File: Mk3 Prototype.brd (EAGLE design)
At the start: 107 x 53.5 mm, 132 parts, among them IC1 STM32F401R, IC2 CC3100, IC3 S25FL216K0PMFI011, J1 ZX62-AB-5PA(11), J2 SWD_SHROUD_SMD, J4 Arduino Headers, J7 SFV30R-2STE1HLF, Q1 BSS84W, Q10 2N7002KW, Q11 BSS84W, Q12 2N7002KW, U1 USD-SOCKETNEW, U2 JHD12864-G13BSW-OUTLINE, U3 MCP73831, X1 ABS07-32.768KHZ-T, X2 Q24FA20H00396, X3 CRYSTAL-3.2-2.5, X4 ABS07-32.768KHZ-T, Y1 AH316M245001-T

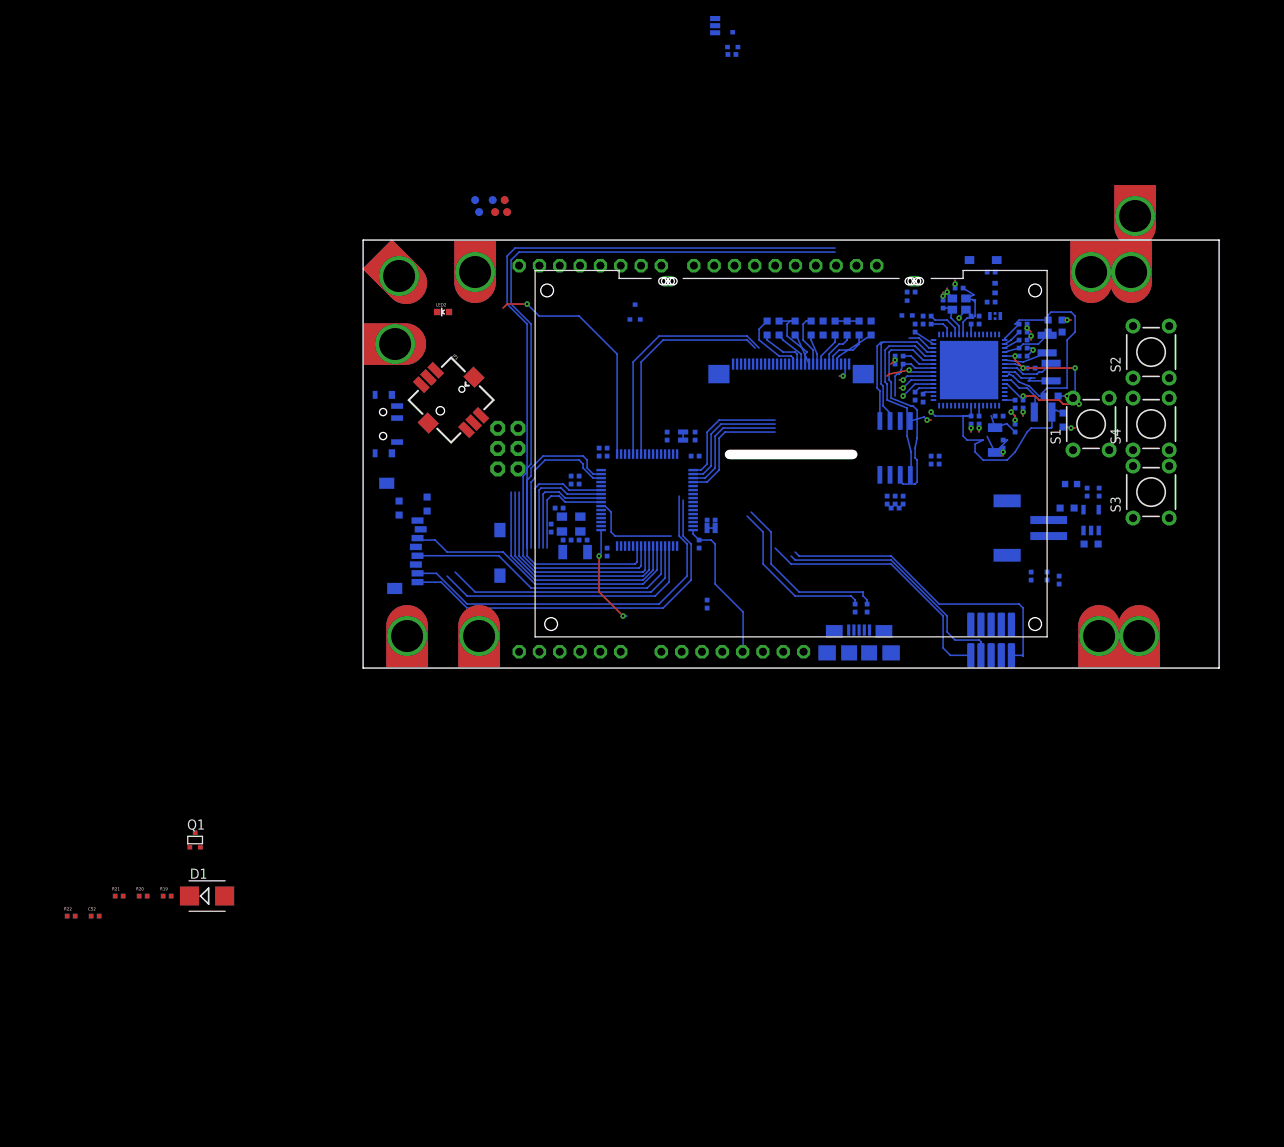
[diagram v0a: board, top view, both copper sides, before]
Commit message: Lots of schematic clean up
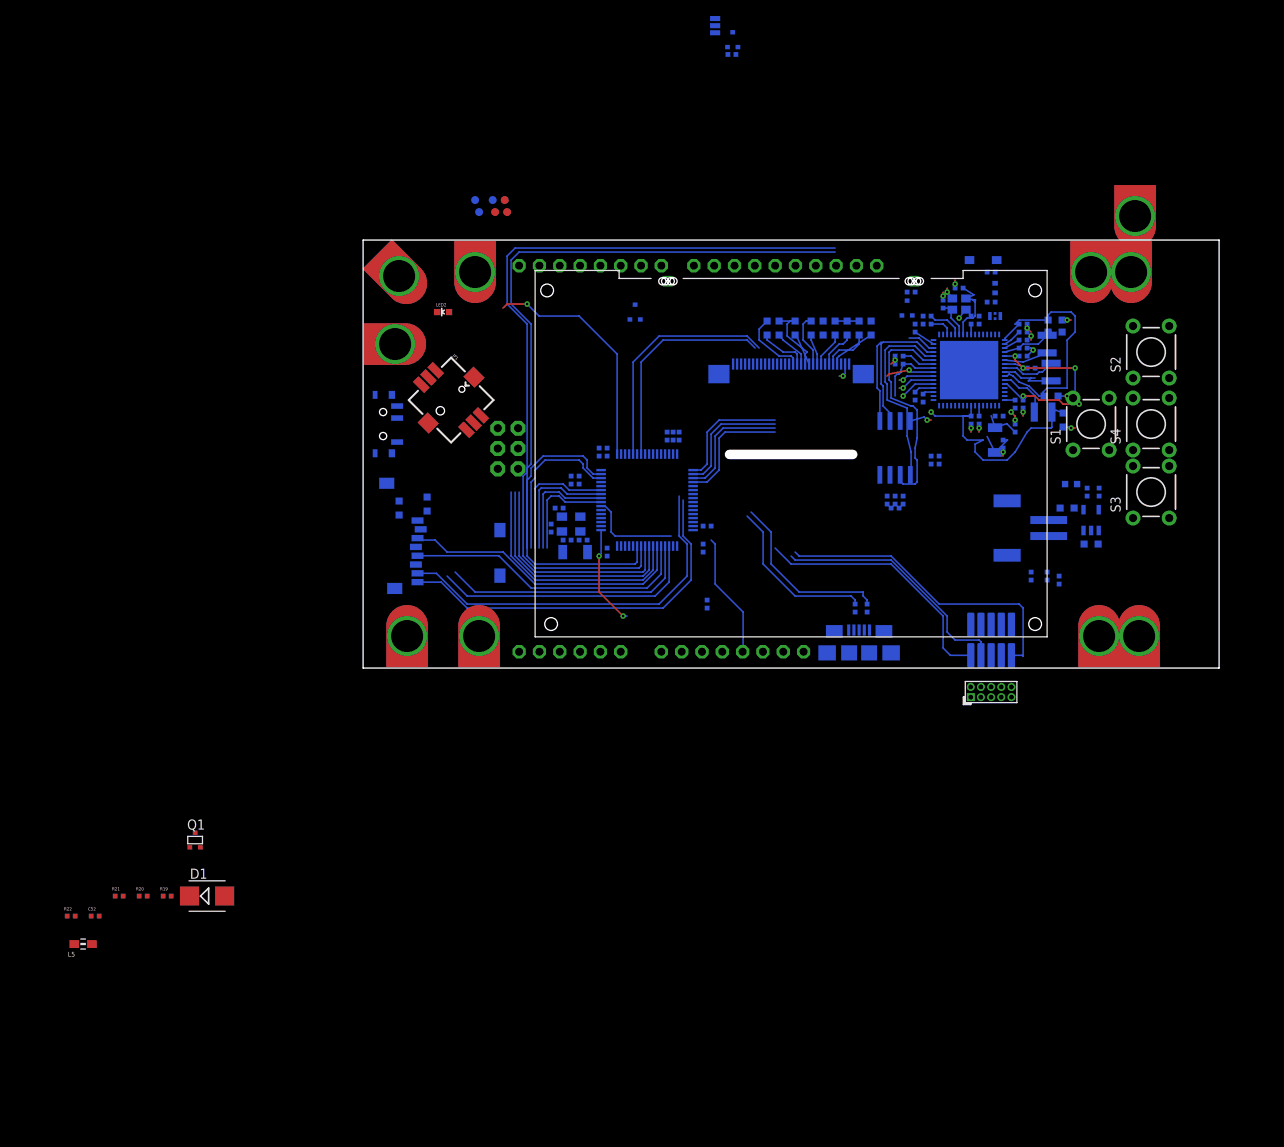
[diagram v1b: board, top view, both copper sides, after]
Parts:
- removed SJ1, SJ2: SOLDERJUMPERTRACE, TiLDA Mk3 Parts:SJ_2S-TRACE
- added JP3: (no value), TiLDA Mk3 Parts:PINHEAD_2X05_127
- added L5: Bead, TiLDA Mk3 Parts:WUERTH-0805
- C34: value 1u -> 0402/1u/10V/X5R
- C35, C36: value 12p -> 0402/12p/50V/NP0
- C48, C49: value nc -> 0402/0R
- R12, R13, R14: value 100K -> 0402/100K/5%
- moved C7 13.7 mm to (39.5, 29.0), turned to 270 degrees
- moved C9 11.5 mm to (42.5, 15.0), turned to 90 degrees
- moved C49 11.5 mm to (38.8, 29.0), turned to 270 degrees
- moved C48 11.3 mm to (43.0, 17.8), turned to 0 degrees
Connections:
- net DM renamed D_N
- net DP renamed D_P
- net N$29 renamed USB_D_N
- net N$30 renamed USB_D_P
- net N$43 renamed OCS32_IN
- net N$45 renamed OCS32_OUT
- new net N$29: L5.1
- new net N$30: IC1.43
- new net N$39: IC1.22
- new net N$43: IC1.24
- new net N$45: IC1.25
- new net N$48: IC1.20
- new net N$49: IC1.16
- new net N$50: IC1.50
- new net N$51: IC1.27
- new net N$52: IC1.28
- new net N$53: IC1.61
- new net N$54: IC1.29
- new net N$55: IC1.37
- new net N$56: IC1.38
- new net VBATT_IN: C34.2, IC1.1, R12.1, R13.1
- net BOOT0: now also R14.2; no longer R14.1
- net GND: now also C10.1, C34.1, R12.2, R14.1; no longer C10.2, C34.2, R12.1, R14.2, SJ1.1, SJ2.1
- net N$13: now also L5.2
- net N$32: now also IC1.42; no longer C34.1, IC1.1, R12.2, R13.1
- net N$37: now also IC1.47; no longer IC1.31, SJ1.2
- net N$38: now also IC1.31; no longer IC1.47, SJ2.2
- net N$4: now also C10.2; no longer C10.1
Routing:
- net VBATT_IN: track 0.00 -> 12.6 mm, vias 0 -> 2
- net N$32: track 12.6 -> 0.00 mm, vias 2 -> 0
- net +3V3: track 18.7 -> 15.6 mm

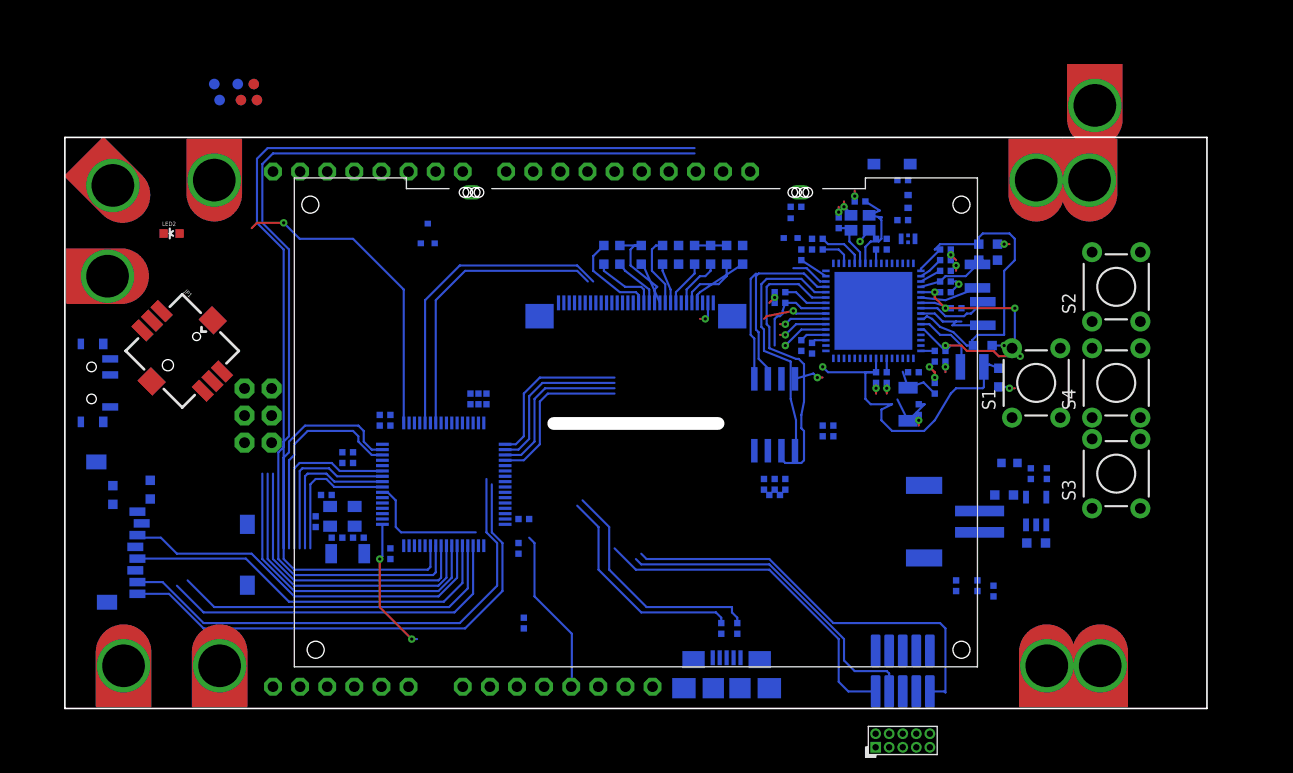
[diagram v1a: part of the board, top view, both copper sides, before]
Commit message: making board symmetrical
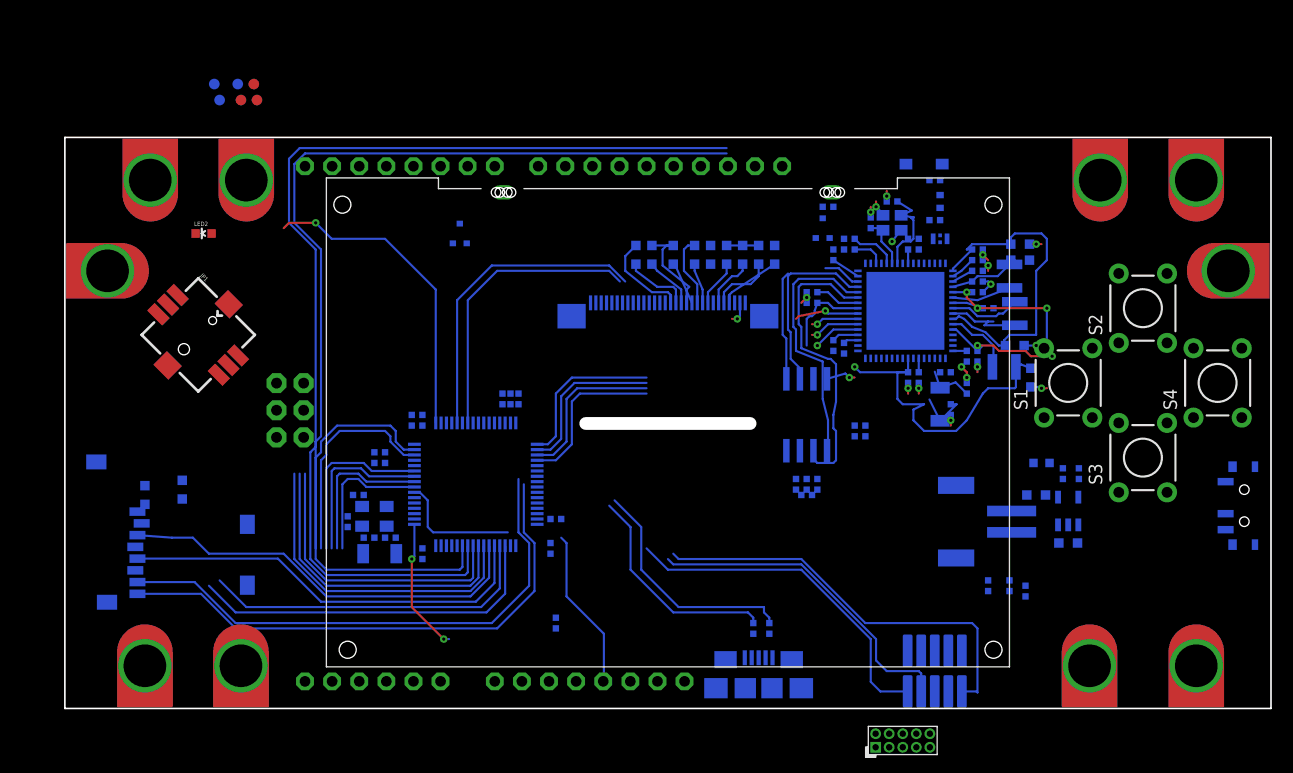
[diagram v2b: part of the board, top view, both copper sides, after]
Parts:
- moved S5 108.6 mm to (110.5, 19.0), turned to 90 degrees
- moved TP8 19.9 mm to (109.0, 41.0), turned to 270 degrees
- moved TP4 10.0 mm to (106.0, 49.5)
- moved S4 9.50 mm to (108.0, 30.5)
- moved TP10 9.00 mm to (106.0, 4.00)
- moved TP1 6.00 mm to (97.0, 49.5)
- moved TP9 4.00 mm to (96.0, 4.00)
- moved TP2 3.54 mm to (8.00, 49.5), turned to 0 degrees
- moved S2 3.20 mm to (101.0, 37.5)
- moved J4 3.04 mm to (86.0, 0.00)
- moved C1 3.00 mm to (81.5, 45.8)
- moved C10 3.00 mm to (41.0, 29.0)
- moved C11 3.00 mm to (83.0, 28.0)
- moved C12 3.00 mm to (84.5, 30.0)
- moved C13 3.00 mm to (75.5, 45.5)
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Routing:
- net SDIO_D1: track 47.4 -> 50.4 mm
- net SDIO_D0: track 47.2 -> 50.2 mm
- net SDIO_CLK: track 36.3 -> 39.3 mm
- net SDIO_CMD: track 36.1 -> 39.0 mm
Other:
- board size 107 x 53.5 mm -> 113 x 53.5 mm
